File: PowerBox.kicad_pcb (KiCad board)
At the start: 2 copper layers, 71.1 x 76.2 mm, 7 parts, among them J1 Screw_Terminal_01x16, U1 MP1584EN, U2 MP1584EN, U3 MP1584EN, U4 MP1584EN, U5 MP1584EN, U6 MP1584EN

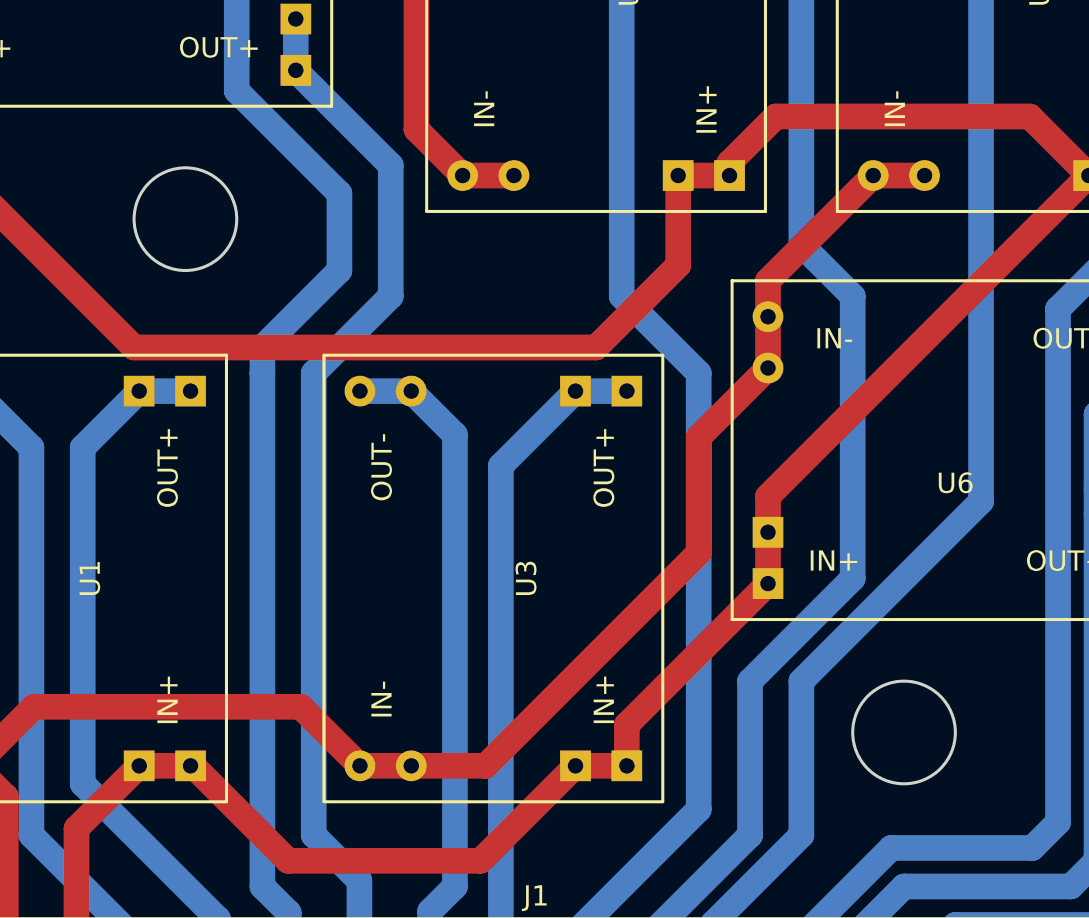
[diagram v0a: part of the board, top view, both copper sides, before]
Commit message: replaced screw holes with custom large through hole pads
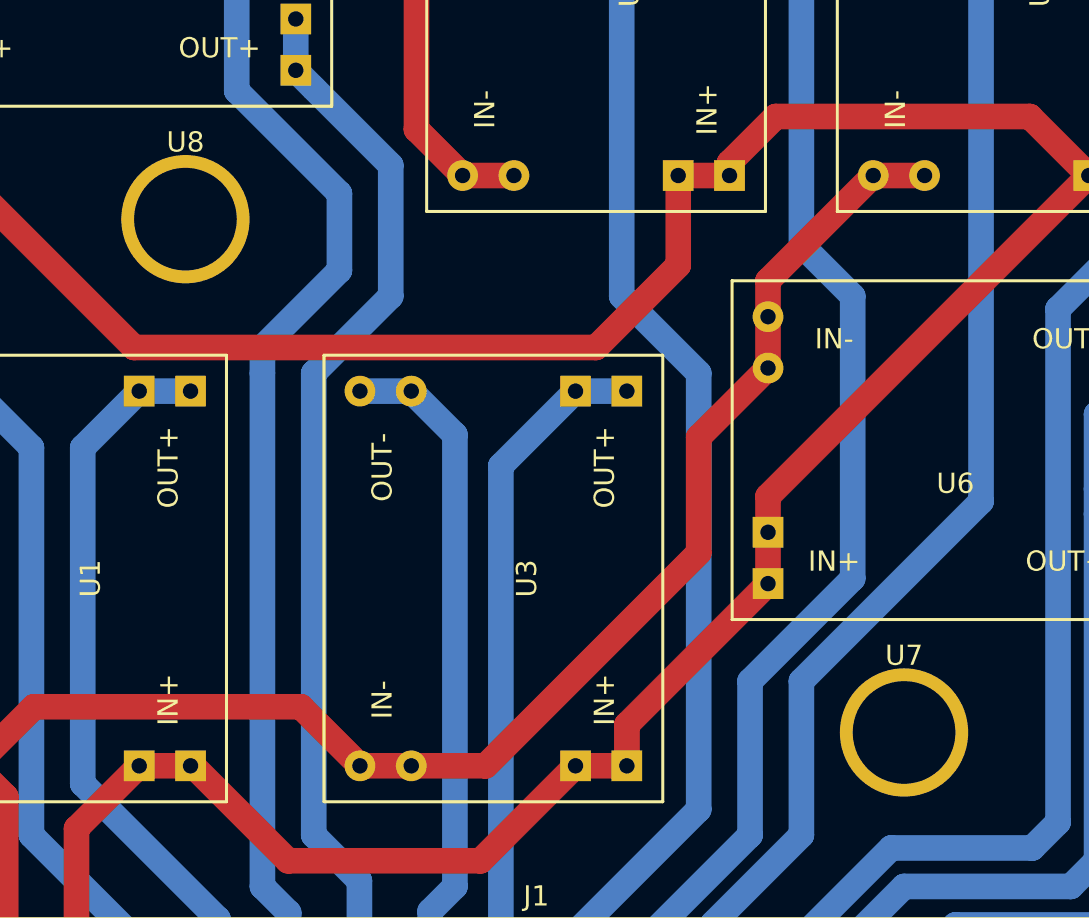
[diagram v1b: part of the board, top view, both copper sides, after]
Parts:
- added U7: SCREW_HOLE, footprints:SCREW_HOLE_0.2in-dia, F.Cu at (154.9, 101.6)
- added U8: SCREW_HOLE, footprints:SCREW_HOLE_0.2in-dia, F.Cu at (119.4, 76.2)
- U1, U2, U3, U4, U5, U6: footprint footprints:MP1584EN_TEXT -> footprints:MP1584EN
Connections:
- J1 pad 1: Net-(J1-Pad1) -> (no net)
- J1 pad 10: Net-(J1-Pad10) -> (no net)
- J1 pad 11: Net-(J1-Pad11) -> (no net)
- J1 pad 12: Net-(J1-Pad12) -> (no net)
- J1 pad 13: Net-(J1-Pad13) -> (no net)
- J1 pad 14: Net-(J1-Pad14) -> (no net)
- J1 pad 15: Net-(J1-Pad15) -> (no net)
- J1 pad 16: Net-(J1-Pad15) -> (no net)
- J1 pad 2: Net-(J1-Pad2) -> (no net)
- J1 pad 3: Net-(J1-Pad3) -> (no net)
- J1 pad 4: Net-(J1-Pad4) -> (no net)
- J1 pad 5: Net-(J1-Pad5) -> (no net)
- J1 pad 6: Net-(J1-Pad6) -> (no net)
- J1 pad 7: Net-(J1-Pad7) -> (no net)
- J1 pad 8: Net-(J1-Pad8) -> (no net)
- J1 pad 9: Net-(J1-Pad9) -> (no net)
- U1 pad 1: Net-(J1-Pad2) -> Net-(U1-Pad1)
- U1 pad 2: Net-(J1-Pad1) -> Net-(U1-Pad2)
- U1 pad 3: Net-(J1-Pad4) -> Net-(U1-Pad3)
- U1 pad 4: Net-(J1-Pad3) -> Net-(U1-Pad4)
- U2 pad 1: Net-(J1-Pad2) -> Net-(U1-Pad1)
- U2 pad 2: Net-(J1-Pad1) -> Net-(U1-Pad2)
- U2 pad 3: Net-(J1-Pad6) -> Net-(U2-Pad3)
- U2 pad 4: Net-(J1-Pad5) -> Net-(U2-Pad4)
- U3 pad 1: Net-(J1-Pad2) -> Net-(U1-Pad1)
- U3 pad 2: Net-(J1-Pad1) -> Net-(U1-Pad2)
- U3 pad 3: Net-(J1-Pad8) -> Net-(U3-Pad3)
- U3 pad 4: Net-(J1-Pad7) -> Net-(U3-Pad4)
- U4 pad 1: Net-(J1-Pad2) -> Net-(U1-Pad1)
- U4 pad 2: Net-(J1-Pad1) -> Net-(U1-Pad2)
- U4 pad 3: Net-(J1-Pad10) -> Net-(U4-Pad3)
- U4 pad 4: Net-(J1-Pad9) -> Net-(U4-Pad4)
- U5 pad 1: Net-(J1-Pad2) -> Net-(U1-Pad1)
- U5 pad 2: Net-(J1-Pad1) -> Net-(U1-Pad2)
- U5 pad 3: Net-(J1-Pad12) -> Net-(U5-Pad3)
- U5 pad 4: Net-(J1-Pad11) -> Net-(U5-Pad4)
- U6 pad 1: Net-(J1-Pad2) -> Net-(U1-Pad1)
- U6 pad 2: Net-(J1-Pad1) -> Net-(U1-Pad2)
- U6 pad 3: Net-(J1-Pad14) -> Net-(U6-Pad3)
- U6 pad 4: Net-(J1-Pad13) -> Net-(J1-Pad6-)
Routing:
- net Net-(U1-Pad2): track 0.00 -> 171.1 mm
- net Net-(J1-Pad1): track 171.1 -> 0.00 mm
- net Net-(U1-Pad1): track 0.00 -> 158.4 mm
- net Net-(J1-Pad2): track 158.4 -> 0.00 mm
- net Net-(U5-Pad3): track 0.00 -> 76.3 mm
- net Net-(J1-Pad12): track 76.3 -> 0.00 mm
- net Net-(U4-Pad3): track 0.00 -> 69.3 mm
- net Net-(J1-Pad10): track 69.3 -> 0.00 mm
- net Net-(U4-Pad4): track 0.00 -> 68.4 mm
- net Net-(J1-Pad9): track 68.4 -> 0.00 mm
- net Net-(U5-Pad4): track 0.00 -> 68.1 mm
- net Net-(J1-Pad11): track 68.1 -> 0.00 mm
- net Net-(U2-Pad4): track 0.00 -> 64.1 mm
- net Net-(J1-Pad5): track 64.1 -> 0.00 mm
- net Net-(U2-Pad3): track 0.00 -> 52.5 mm
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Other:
- outline, holes or cut-outs redrawn
